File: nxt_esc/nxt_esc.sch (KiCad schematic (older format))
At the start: 18 parts, among them IC1 L293D, J1 NXT_MOTOR, J2 NXT_MOTOR, SW1 Skid Steer/Drive & Steer, SW2 Center Steering, SW3 SPST, U1 LM7805CT

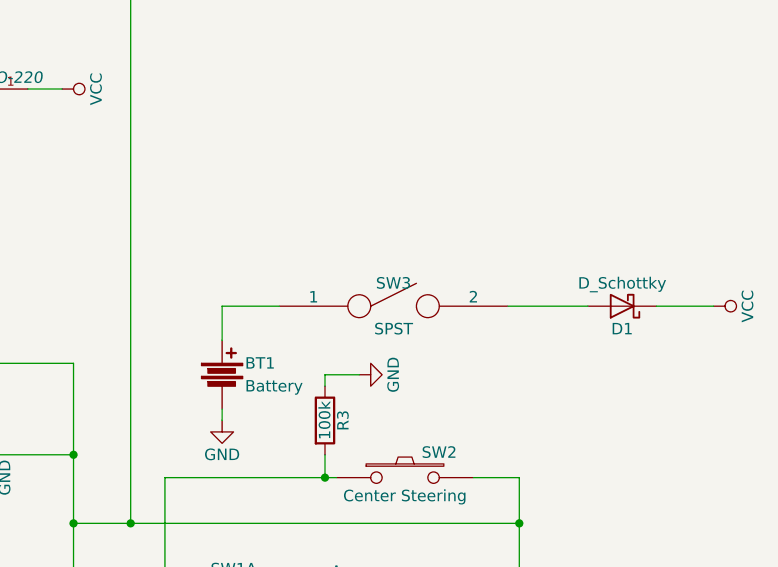
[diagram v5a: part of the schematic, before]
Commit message: Updated components to ones I already have
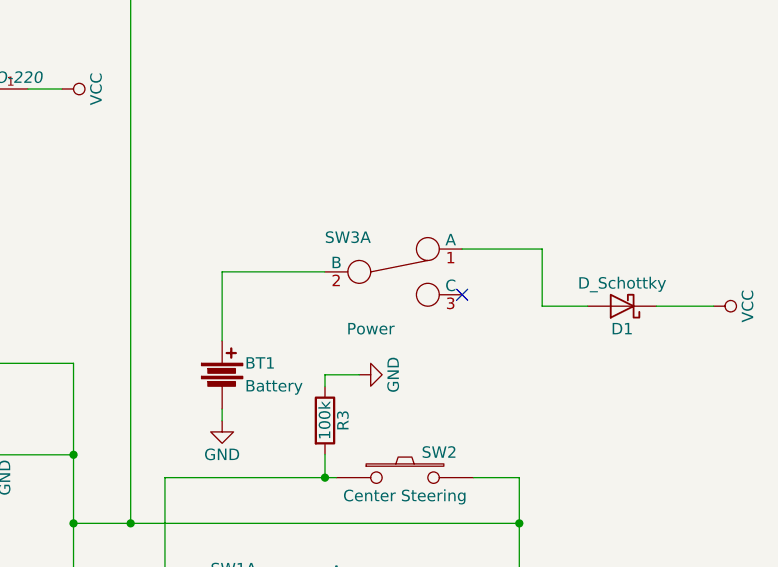
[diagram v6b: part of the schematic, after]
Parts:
- removed SW3: SPST, Buttons_Switches_ThroughHole:SW_DIP_x1_W7.62mm_Slide, symbol SPST
- added SW3: Power, nxt_sec_lib:SLIDE_SWITCH_JRL, symbol Switch_SPDT_x2
- BT1: footprint Terminal_Blocks:TerminalBlock_bornier-2_P5.08mm -> nxt_sec_lib:SCREW_TERMINAL_JRL
- SW1: footprint Buttons_Switches_ThroughHole:SW_CuK_OS102011MA1QN1_SPDT_Angled -> nxt_sec_lib:SLIDE_SWITCH_JRL
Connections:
- net at BT1.1: now also SW3.2 (B)
- net at D1.2 (A): now also SW3.1 (A)
- no-connect marks 11 -> 12
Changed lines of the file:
@@
 F 0 "BT1" H 8150 2800 50  0000 L CNN
 F 1 "Battery" H 8150 2700 50  0000 L CNN
-F 2 "Terminal_Blocks:TerminalBlock_bornier-2_P5.08mm" V 8050 2790 50  0001 C CNN
+F 2 "nxt_sec_lib:SCREW_TERMINAL_JRL" V 8050 2790 50  0001 C CNN
 F 3 "" V 8050 2790 50  0000 C CNN
 	1    8050 2750
@@
 F 0 "SW1" H 8100 3900 50  0000 C CNN
 F 1 "Skid Steer/Drive & Steer" H 8200 3500 50  0000 C CNN
-F 2 "Buttons_Switches_ThroughHole:SW_CuK_OS102011MA1QN1_SPDT_Angled" H 8300 3750 50  0001 C CNN
+F 2 "nxt_sec_lib:SLIDE_SWITCH_JRL" H 8300 3750 50  0001 C CNN
 F 3 "" H 8300 3750 50  0000 C CNN
 	1    8300 3750
@@
 Connection ~ 9350 3650
 Connection ~ 7650 3400
-Wire Wire Line
-	8050 2600 8050 2450
 $Comp
 L LM7805CT U1
@@
 	-1   0    0    1
 $EndComp
-$Comp
-L SPST SW3
-U 1 1 5AABF253
-P 8800 2450
-F 0 "SW3" H 8800 2550 50  0000 C CNN
-F 1 "SPST" H 8800 2350 50  0000 C CNN
-F 2 "Buttons_Switches_ThroughHole:SW_DIP_x1_W7.62mm_Slide" H 8800 2450 50  0001 C CNN
-F 3 "" H 8800 2450 50  0000 C CNN
-	1    8800 2450
-	1    0    0    -1
-$EndComp
-Wire Wire Line
-	8050 2450 8300 2450
-Wire Wire Line
-	9300 2450 9650 2450
 Wire Wire Line
 	9950 2450 10200 2450
+$Comp
+L Switch_SPDT_x2 SW3
+U 1 1 5AB3DAE7
+P 8800 2300
+F 0 "SW3" H 8600 2450 50  0000 C CNN
+F 1 "Power" H 8700 2050 50  0000 C CNN
+F 2 "nxt_sec_lib:SLIDE_SWITCH_JRL" H 8800 2300 50  0001 C CNN
+F 3 "" H 8800 2300 50  0000 C CNN
+	1    8800 2300
+	1    0    0    -1
+$EndComp
+Wire Wire Line
+	8500 2300 8050 2300
+Wire Wire Line
+	8050 2300 8050 2600
+Wire Wire Line
+	9100 2200 9450 2200
+Wire Wire Line
+	9450 2200 9450 2450
+Wire Wire Line
+	9450 2450 9650 2450
+NoConn ~ 9100 2400
 $EndSCHEMATC

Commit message: Made more room for arduino
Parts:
- BT1: symbol Battery -> Battery-RESCUE-nxt_esc
- RV1: symbol POT -> POT-RESCUE-nxt_esc
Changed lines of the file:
@@
 LIBS:ArduProMiniTKB
 LIBS:L293D
-LIBS:wayne_and_layne_kicad_symbols
 LIBS:nxt_esc-cache
 EELAYER 25 0
@@
 $EndComp
 $Comp
-L Battery BT1
+L Battery-RESCUE-nxt_esc BT1
 U 1 1 5A556E73
 P 8050 2750
@@
 $EndComp
 $Comp
-L POT RV1
+L POT-RESCUE-nxt_esc RV1
 U 1 1 5A557E6E
 P 8250 4750
